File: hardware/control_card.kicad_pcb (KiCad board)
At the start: 6 copper layers, 32.5 x 33.8 mm, 144 parts, among them J1 Power board, J2 JTAG, U1 A3CZ065BB18AE7S, U10 SN74LV4051APWR, U11 OPA365AIDBVR, U12 ADS7056IRUGR, U13 SN74LV4051APWR, U14 OPA365AIDBVR, U15 ADS7056IRUGR, U16 TLV75518PDBVR, U2 AP61302Z6-7, U3 AP61102Z6-7, U4 AP61102Z6-7, U5 TLV75512PDBVR, U6 TLV75533PDBVR, U7 MT25QU256ABA8E12-1SIT, U8 SN74AVC4T774RSVR, U9 W958D8NBYA5I, X1 100MHz

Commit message: J1 pads 0.9 mm: annular ring 0.17 mm (JLC minimum 0.15)
J1's 50 pads were U25's 0.8128 mm on 0.5588 mm drills, a 0.127 mm annular
ring, below JLC's multilayer minimum of 0.15 mm (production-checklist
review). Pads enlarged to 0.9 mm in the footprint and on the board; drills
unchanged. Tracks between the pins still clear: closest pad-to-track
0.109 mm, hole-to-copper 0.28 mm. DRC: 0 errors, 0 unconnected, 0 parity.

Co-Authored-By: Claude Opus 5.5 <noreply@anthropic.com>
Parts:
- moved C63 1.70 mm to (82.0, 119.5), turned to 90 degrees
- moved C14 0.52 mm to (99.6, 124.0)
- moved C15 0.51 mm to (95.6, 124.0)
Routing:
- net +5V: track 81.1 -> 76.2 mm
- net +3V3: track 24.8 -> 20.5 mm
- net +3V3A: track 46.0 -> 42.3 mm
- net GND: track 70.0 -> 68.0 mm, vias 178 -> 179

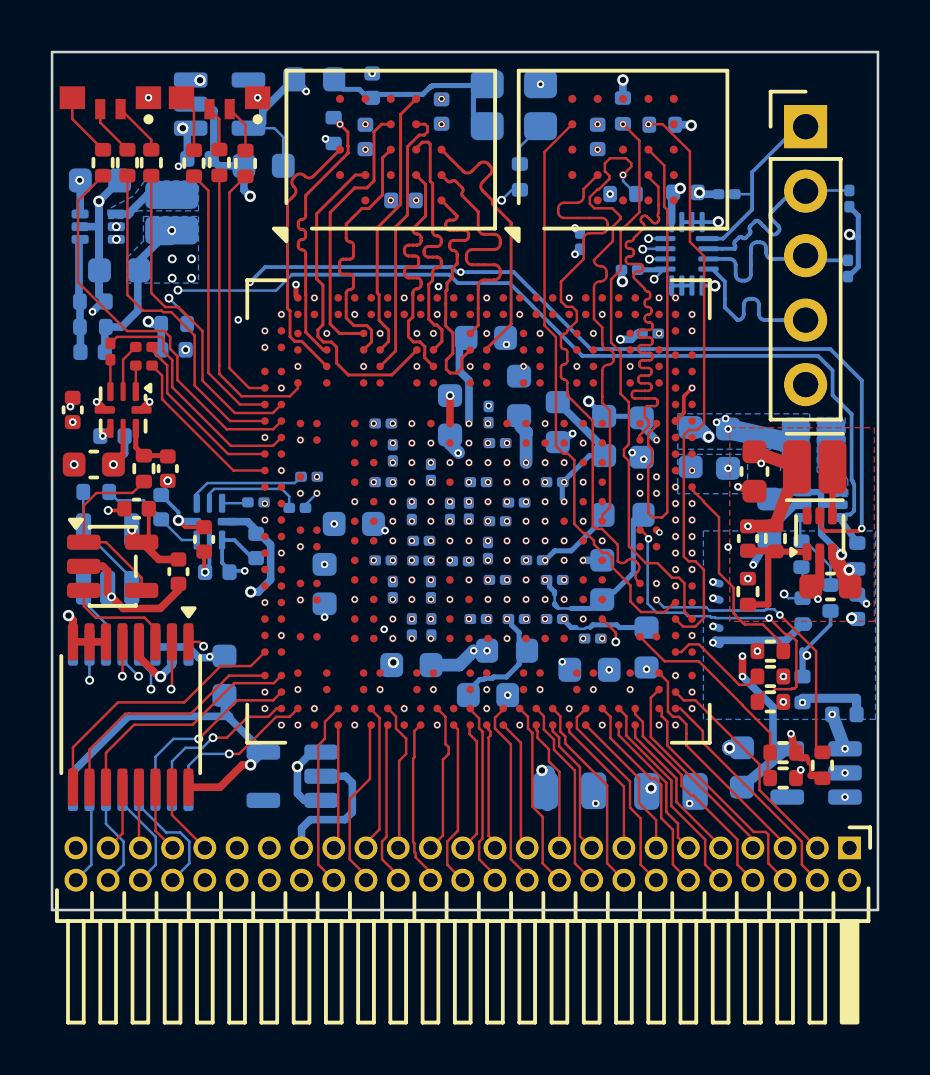
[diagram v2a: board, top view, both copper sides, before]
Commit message: Design-review fixes: core buck feed-forward, EPWM2A/B pull-downs, mux bypass
From the pre-order design review:
- C77 120 pF C0G (C40059) across R1, VCC_SENSE_P to FB_0V75: the AP61302
  datasheet requires a feed-forward cap (33 pF with a 200k top resistor;
  scaled for R1 = 49.9k).
- C4, C7 22 pF -> 33 pF (C1562), the AP61102 datasheet value for these
  dividers.
- R40, R41 10k 0201 pull-downs on EPWM2A / EPWM2B. These drive the power
  board's Si8661 isolator inputs, which have no pull-down there; the other
  PWM lines already have 10k pull-downs on the power board.
- C78, C79 100 nF extra +3V3A bypass for the muxes (C79 is placed near U14;
  move it to U13 pin 16 if it's meant for U13).
Parts placed by hand; new reference text hidden like the rest.

DRC: 0 errors, 0 unconnected, 0 parity issues. BOM 44 lines / 146 parts;
all parts orderable for 10 boards (tightest ADS7056, 29).

Co-Authored-By: Claude Opus 5.5 <noreply@anthropic.com>
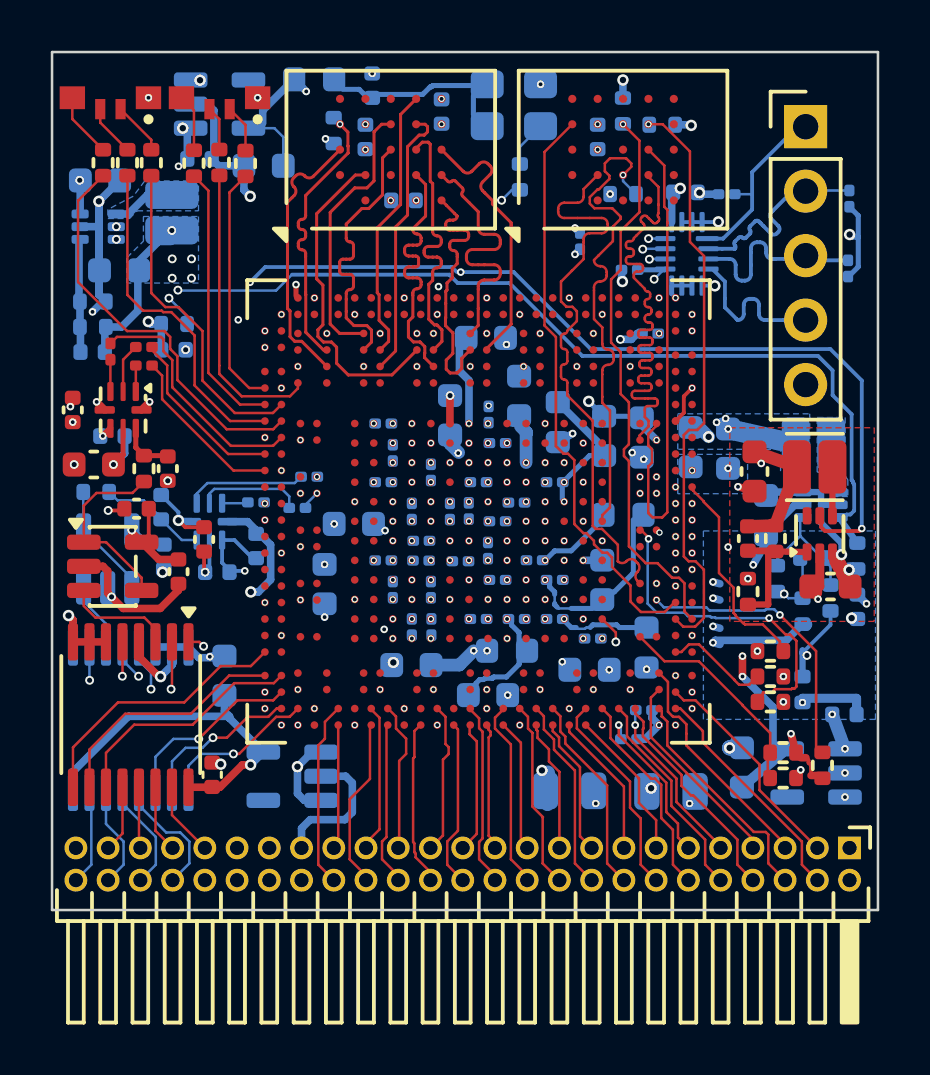
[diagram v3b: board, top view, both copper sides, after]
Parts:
- added C77: 120p, Capacitor_SMD:C_0402_1005Metric, B.Cu at (105.2, 114.8)
- added C78: 100n, Capacitor_SMD:C_0402_1005Metric, F.Cu at (81.5, 123.4)
- added C79: 100n, Capacitor_SMD:C_0402_1005Metric, B.Cu at (79.6, 114.8)
- added R40: 10k, Resistor_SMD:R_0201_0603Metric, B.Cu at (98.5, 120.8)
- added R41: 10k, Resistor_SMD:R_0201_0603Metric, B.Cu at (97.9, 122.0)
- C4, C7: value 22p -> 33p
- moved R1 1.36 mm to (103.8, 115.6)
- moved C1 0.19 mm to (103.3, 113.1)
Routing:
- net GND: track 68.0 -> 70.3 mm, vias 179 -> 181
- net /Power/FB_0V75: track 3.20 -> 4.75 mm
- net +3V3A: track 42.3 -> 43.8 mm
- net EPWM2A: track 6.23 -> 6.83 mm, vias 0 -> 1
- net EPWM2B: track 5.98 -> 6.57 mm, vias 0 -> 1
- net +3V3: vias 30 -> 29

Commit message: BOM: secure 680p stock, two extended parts to basic
- C56, C61 (680 pF C0G kickback): 0402CG681J500NT (C301953, 78 orderable)
  -> Yageo CC0402JRNPO9BN681 (C113781, 57063 orderable), same spec.
- C77 core feed-forward 120 pF (C40059, extended) -> 100 pF C0G basic
  (C1546); zero moves from 24 to 31 kHz.
- R1 core divider top 49.9k (C137969, extended) -> 51k basic (C25794);
  core output 0.750 -> 0.753 V (+0.4 %, FPGA allows +/-3 %).
Extended part types 25 -> 23. Schematic and board updated together;
docs updated for 51k/0.753 V. Five symbols added earlier re-indented.

DRC: 0 errors, 0 unconnected, 0 parity issues. ERC: GNDSENSE only.

Co-Authored-By: Claude Opus 5.5 <noreply@anthropic.com>
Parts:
- C77: value 120p -> 100p
- R1: value 49k9 -> 51k
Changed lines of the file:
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@@
 			)
 		)
-		(property "LCSC" "C301953"
+		(property "LCSC" "C113781"
 			(at 0 0 270)
 			(layer "F.Fab")
@@
 			)
 		)
-		(property "MPN" "0402CG681J500NT"
+		(property "MPN" "CC0402JRNPO9BN681"
 			(at 0 0 270)
 			(layer "F.Fab")
@@
 			)
 		)
-		(property "Value" "49k9"
+		(property "Value" "51k"
 			(at 0 -1.17 90)
 			(layer "B.Fab")
@@
 			)
 		)
-		(property "LCSC" "C137969"
+		(property "LCSC" "C25794"
 			(at 0 0 90)
 			(layer "B.Fab")
@@
 			)
 		)
-		(property "MPN" "RC0402FR-0749K9L"
+		(property "MPN" "0402WGF5102TCE"
 			(at 0 0 90)
 			(layer "B.Fab")
@@
 			)
 		)
-		(property "Value" "120p"
+		(property "Value" "100p"
 			(at 0 -1.16 0)
 			(layer "B.Fab")
@@
 			)
 		)
-		(property "LCSC" "C40059"
+		(property "LCSC" "C1546"
 			(at 0 0 180)
 			(unlocked yes)
@@
 			)
 		)
-		(property "MPN" "0402CG121J500NT"
+		(property "MPN" "0402CG101J500NT"
 			(at 0 0 180)
 			(unlocked yes)
@@
 			)
 		)
-		(property "LCSC" "C301953"
+		(property "LCSC" "C113781"
 			(at 0 0 90)
 			(layer "B.Fab")
@@
 			)
 		)
-		(property "MPN" "0402CG681J500NT"
+		(property "MPN" "CC0402JRNPO9BN681"
 			(at 0 0 90)
 			(layer "B.Fab")
